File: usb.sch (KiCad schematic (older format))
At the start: 17 parts, among them J4 CONN_02X03, U1 LFE5U-85F-6BG381C, Y1 FNETHE025

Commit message: Adding default parts
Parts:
- D20, D21, D23, D24, D25, D26: footprint Diode_SMD:D_SOD-323_HandSoldering -> Diode_SMD:D_SOD-323
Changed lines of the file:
@@
 F 0 "D20" H 2800 2900 50  0000 C CNN
 F 1 "3.6V" H 2600 2910 50  0000 C CNN
-F 2 "Diode_SMD:D_SOD-323_HandSoldering" V 2600 3000 50  0001 C CNN
+F 2 "Diode_SMD:D_SOD-323" V 2600 3000 50  0001 C CNN
 F 3 "http://www.taiwansemi.com/products/datasheet/BZT52C2V4S%20SERIES_H1709.pdf" V 2600 3000 50  0001 C CNN
 F 4 "www.taiwansemi.com" H 2600 3000 60  0001 C CNN "MNF1_URL"
@@
 F 0 "D21" H 2900 3100 50  0000 C CNN
 F 1 "3.6V" H 2700 3100 50  0000 C CNN
-F 2 "Diode_SMD:D_SOD-323_HandSoldering" V 2700 3000 50  0001 C CNN
+F 2 "Diode_SMD:D_SOD-323" V 2700 3000 50  0001 C CNN
 F 3 "http://www.taiwansemi.com/products/datasheet/BZT52C2V4S%20SERIES_H1709.pdf" V 2700 3000 50  0001 C CNN
 F 4 "www.taiwansemi.com" H 2700 3000 60  0001 C CNN "MNF1_URL"
@@
 F 0 "D23" H 1650 4950 50  0000 C CNN
 F 1 "1N914" H 1900 4950 50  0000 C CNN
-F 2 "Diode_SMD:D_SOD-323_HandSoldering" V 1950 4850 50  0001 C CNN
+F 2 "Diode_SMD:D_SOD-323" V 1950 4850 50  0001 C CNN
 F 3 "https://www.diodes.com/assets/Datasheets/ds30065.pdf" V 1950 4850 50  0001 C CNN
 	1    1950 4850
@@
 F 0 "D25" H 1650 5550 50  0000 C CNN
 F 1 "1N914" H 1900 5550 50  0000 C CNN
-F 2 "Diode_SMD:D_SOD-323_HandSoldering" V 1950 5450 50  0001 C CNN
+F 2 "Diode_SMD:D_SOD-323" V 1950 5450 50  0001 C CNN
 F 3 "https://www.diodes.com/assets/Datasheets/ds30065.pdf" V 1950 5450 50  0001 C CNN
 	1    1950 5450
@@
 F 0 "D24" H 2250 4750 50  0000 C CNN
 F 1 "1N914" H 1900 4750 50  0000 C CNN
-F 2 "Diode_SMD:D_SOD-323_HandSoldering" V 1950 4650 50  0001 C CNN
+F 2 "Diode_SMD:D_SOD-323" V 1950 4650 50  0001 C CNN
 F 3 "https://www.diodes.com/assets/Datasheets/ds30065.pdf" V 1950 4650 50  0001 C CNN
 	1    1950 4650
@@
 F 0 "D26" H 2250 5350 50  0000 C CNN
 F 1 "1N914" H 1900 5350 50  0000 C CNN
-F 2 "Diode_SMD:D_SOD-323_HandSoldering" V 1950 5250 50  0001 C CNN
+F 2 "Diode_SMD:D_SOD-323" V 1950 5250 50  0001 C CNN
 F 3 "https://www.diodes.com/assets/Datasheets/ds30065.pdf" V 1950 5250 50  0001 C CNN
 F 4 "1N4148WS" H 1950 5250 50  0001 C CNN "MPN"

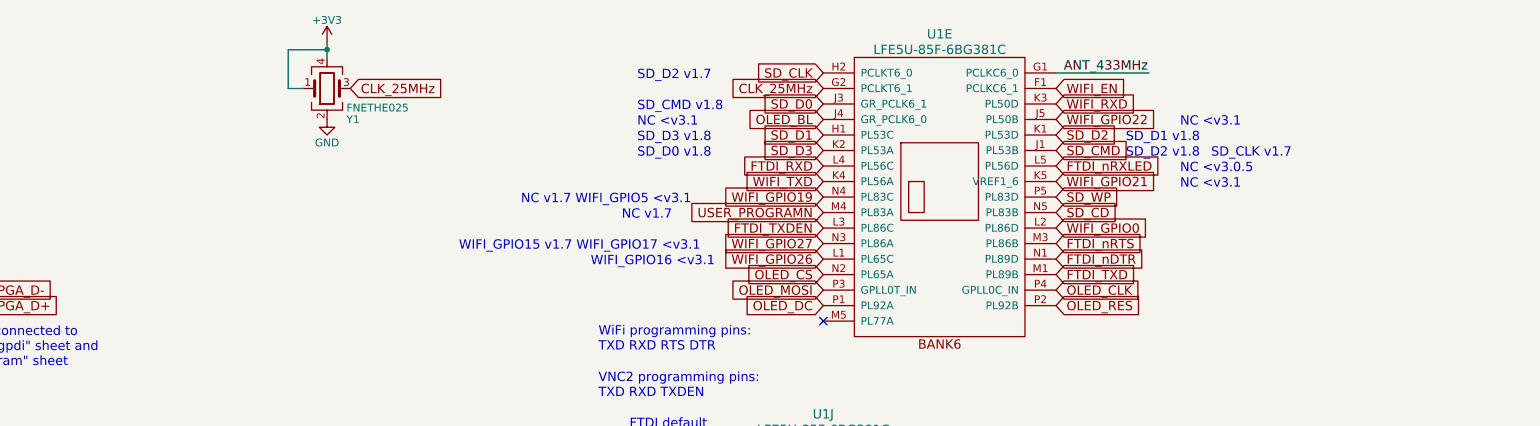
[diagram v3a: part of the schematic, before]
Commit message: Rewiering LCD OUT to bottom left
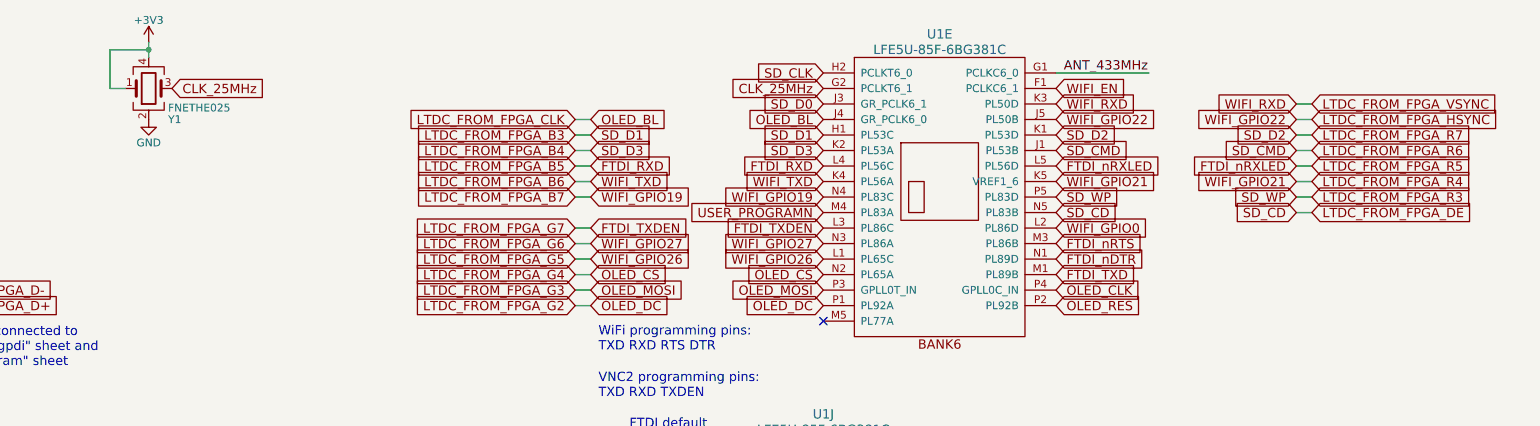
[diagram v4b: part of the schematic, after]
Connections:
- net OLED_BL renamed LTDC_FROM_FPGA_CLK
- net OLED_CS renamed LTDC_FROM_FPGA_G4
- net OLED_DC renamed LTDC_FROM_FPGA_G2
- net OLED_MOSI renamed LTDC_FROM_FPGA_G3
- net SD_CD renamed LTDC_FROM_FPGA_DE
- net SD_CMD renamed LTDC_FROM_FPGA_R6
- net SD_D1 renamed LTDC_FROM_FPGA_B3
- net SD_D2 renamed LTDC_FROM_FPGA_R7
- net SD_D3 renamed LTDC_FROM_FPGA_B4
- net SD_WP renamed LTDC_FROM_FPGA_R3
- net WIFI_GPIO19 renamed LTDC_FROM_FPGA_B7
- net WIFI_GPIO21 renamed LTDC_FROM_FPGA_R4
- net WIFI_GPIO22 renamed LTDC_FROM_FPGA_HSYNC
- net WIFI_GPIO26 renamed LTDC_FROM_FPGA_G5
- net WIFI_GPIO27 renamed LTDC_FROM_FPGA_G6
- net WIFI_RXD renamed LTDC_FROM_FPGA_VSYNC
- net WIFI_TXD renamed LTDC_FROM_FPGA_B6
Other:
- note removed: "NC <v3.0.5"
- note removed: "NC <v3.1"
- note removed: "NC v1.7"
- note removed: "NC v1.7 WIFI_GPIO5 <v3.1"
- note removed: "SD_CLK v1.7"
- note removed: "SD_CMD v1.8"
- note removed: "SD_D0 v1.8"
- note removed: "SD_D1 v1.8"
- note removed: "SD_D2 v1.7"
- note removed: "SD_D2 v1.8"
- note removed: "SD_D3 v1.8"
- note removed: "WIFI_GPIO15 v1.7 WIFI_GPIO17 <v3.1"
- note removed: "WIFI_GPIO16 <v3.1"
- moved on the sheet: Y1
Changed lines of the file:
@@
 L Device:Crystal_GND24 Y1
 U 1 1 5A079883
-P 5450 1450
-F 0 "Y1" H 5575 1650 50  0000 L CNN
-F 1 "FNETHE025" H 5575 1575 50  0000 L CNN
-F 2 "oscxo:Crystal_SMD_7050_4Pads" H 5450 1450 50  0001 C CNN
-F 3 "https://www.diodes.com/assets/Datasheets/FNETHE025.pdf" H 5450 1450 50  0001 C CNN
-F 4 "www.diodes.com" H 5450 1450 60  0001 C CNN "MNF1_URL"
-F 5 "FNETHE025" H 5450 1450 60  0001 C CNN "MPN"
-F 6 "SiT8008BC-81-33E-25.000000X" H 5450 1450 50  0001 C CNN "MPN2"
-F 7 "https://datasheet.lcsc.com/szlcsc/1912111437_Shenzhen-SCTF-Elec-S7D25-000000D20F30T_C387026.pdf" H 5450 1450 50  0001 C CNN "MNF3_URL"
-F 8 "S7D25.000000D20F30T" H 5450 1450 50  0001 C CNN "MPN3"
-F 9 "729-FNETHE025" H 5450 1450 60  0001 C CNN "Mouser"
-F 10 "788-8008BC8133E25X " H 5450 1450 50  0001 C CNN "Mouse_r2"
-F 11 "FNETHE025CT-ND" H 5450 1450 50  0001 C CNN "Digikey"
-F 12 "C390569" H 5450 1450 50  0001 C CNN "LCSC"
-F 13 "0.7942$" H 5450 1450 50  0001 C CNN "price100_Digikey"
-F 14 "FQ001" H 5450 1450 50  0001 C CNN "Koncar"
-F 15 "T" H 5450 1450 50  0001 C CNN "Side"
-	1    5450 1450
+P 4300 1450
+F 0 "Y1" H 4425 1650 50  0000 L CNN
+F 1 "FNETHE025" H 4425 1575 50  0000 L CNN
+F 2 "oscxo:Crystal_SMD_7050_4Pads" H 4300 1450 50  0001 C CNN
+F 3 "https://www.diodes.com/assets/Datasheets/FNETHE025.pdf" H 4300 1450 50  0001 C CNN
+F 4 "www.diodes.com" H 4300 1450 60  0001 C CNN "MNF1_URL"
+F 5 "FNETHE025" H 4300 1450 60  0001 C CNN "MPN"
+F 6 "SiT8008BC-81-33E-25.000000X" H 4300 1450 50  0001 C CNN "MPN2"
+F 7 "https://datasheet.lcsc.com/szlcsc/1912111437_Shenzhen-SCTF-Elec-S7D25-000000D20F30T_C387026.pdf" H 4300 1450 50  0001 C CNN "MNF3_URL"
+F 8 "S7D25.000000D20F30T" H 4300 1450 50  0001 C CNN "MPN3"
+F 9 "729-FNETHE025" H 4300 1450 60  0001 C CNN "Mouser"
+F 10 "788-8008BC8133E25X " H 4300 1450 50  0001 C CNN "Mouse_r2"
+F 11 "FNETHE025CT-ND" H 4300 1450 50  0001 C CNN "Digikey"
+F 12 "C390569" H 4300 1450 50  0001 C CNN "LCSC"
+F 13 "0.7942$" H 4300 1450 50  0001 C CNN "price100_Digikey"
+F 14 "FQ001" H 4300 1450 50  0001 C CNN "Koncar"
+F 15 "T" H 4300 1450 50  0001 C CNN "Side"
+	1    4300 1450
 	1    0    0    1
 $EndComp
 Wire Wire Line
-	5450 1150 5450 1200
-Wire Wire Line
-	5300 1450 5200 1450
-Wire Wire Line
-	5200 1450 5200 1200
-Wire Wire Line
-	5200 1200 5450 1200
-Connection ~ 5450 1200
+	4300 1150 4300 1200
+Wire Wire Line
+	4150 1450 4050 1450
+Wire Wire Line
+	4050 1450 4050 1200
+Wire Wire Line
+	4050 1200 4300 1200
+Connection ~ 4300 1200
 $Comp
 L power:GND #PWR0110
 U 1 1 5A07A1D3
-P 5450 1650
-F 0 "#PWR0110" H 5450 1400 50  0001 C CNN
-F 1 "GND" H 5450 1500 50  0000 C CNN
-F 2 "" H 5450 1650 50  0001 C CNN
-F 3 "" H 5450 1650 50  0001 C CNN
-	1    5450 1650
+P 4300 1650
+F 0 "#PWR0110" H 4300 1400 50  0001 C CNN
+F 1 "GND" H 4300 1500 50  0000 C CNN
+F 2 "" H 4300 1650 50  0001 C CNN
+F 3 "" H 4300 1650 50  0001 C CNN
+	1    4300 1650
 	1    0    0    -1
 $EndComp
-Text GLabel 5600 1450 2    60   Input ~ 0
+Text GLabel 4450 1450 2    60   Input ~ 0
 CLK_25MHz
 $Comp
 L power:+3V3 #PWR0109
 U 1 1 5A07A3D1
-P 5450 1150
-F 0 "#PWR0109" H 5450 1000 50  0001 C CNN
-F 1 "+3V3" H 5450 1290 50  0000 C CNN
-F 2 "" H 5450 1150 50  0001 C CNN
-F 3 "" H 5450 1150 50  0001 C CNN
-	1    5450 1150
+P 4300 1150
+F 0 "#PWR0109" H 4300 1000 50  0001 C CNN
+F 1 "+3V3" H 4300 1290 50  0000 C CNN
+F 2 "" H 4300 1150 50  0001 C CNN
+F 3 "" H 4300 1150 50  0001 C CNN
+	1    4300 1150
 	1    0    0    -1
 $EndComp
-Text Notes 6300 2500 0    60   ~ 0
-WIFI_GPIO15 v1.7 WIFI_GPIO17 <v3.1
 Text GLabel 8650 2150 0    60   Input ~ 0
 WIFI_GPIO19
 Text GLabel 8650 2450 0    60   Input ~ 0
 WIFI_GPIO27
-Text Notes 7450 1400 0    60   ~ 0
-SD_D2 v1.7
-Text Notes 11150 1900 0    60   ~ 0
-SD_CLK v1.7
 Text GLabel 1600 4850 0    60   Input ~ 0
 USB_FPGA_PULL_D+
@@
 	2700 2750 3000 2750
 Wire Wire Line
-	5450 1200 5450 1250
+	4300 1200 4300 1250
 Wire Wire Line
 	2550 4850 2750 4850
@@
 Text Label 1850 2650 0    60   ~ 0
 US2VBUS
-Text Notes 10600 1900 0    60   ~ 0
-SD_D2 v1.8
-Text Notes 10600 1800 0    60   ~ 0
-SD_D1 v1.8
-Text Notes 7450 1600 0    60   ~ 0
-SD_CMD v1.8
-Text Notes 7450 1800 0    60   ~ 0
-SD_D3 v1.8
-Text Notes 7450 1900 0    60   ~ 0
-SD_D0 v1.8
 Text GLabel 8650 1750 0    60   Input ~ 0
 SD_D1
@@
 Text GLabel 8650 2250 0    60   Input ~ 0
 USER_PROGRAMN
-Text Notes 7350 2300 0    60   ~ 0
-NC v1.7
 NoConn ~ 8650 2950
 Text GLabel 10150 1950 2    60   Input ~ 0
 FTDI_nRXLED
-Text Notes 10950 2000 0    60   ~ 0
-NC <v3.0.5
-Text Notes 6700 2200 0    60   ~ 0
-NC v1.7 WIFI_GPIO5 <v3.1
 Text GLabel 10150 2050 2    60   Input ~ 0
 WIFI_GPIO21
-Text Notes 10950 2100 0    60   ~ 0
-NC <v3.1
 Text GLabel 10150 1650 2    60   Input ~ 0
 WIFI_GPIO22
-Text Notes 10950 1700 0    60   ~ 0
-NC <v3.1
 Text GLabel 8650 1650 0    60   Input ~ 0
 OLED_BL
-Text Notes 7450 1700 0    60   ~ 0
-NC <v3.1
-Text Notes 7150 2600 0    60   ~ 0
-WIFI_GPIO16 <v3.1
+Text GLabel 7050 1750 0    60   Input ~ 0
+LTDC_FROM_FPGA_B3
+Text GLabel 7050 1850 0    60   Input ~ 0
+LTDC_FROM_FPGA_B4
+Text GLabel 7050 1950 0    60   Input ~ 0
+LTDC_FROM_FPGA_B5
+Text GLabel 7050 2050 0    60   Input ~ 0
+LTDC_FROM_FPGA_B6
+Text GLabel 7050 2150 0    60   Input ~ 0
+LTDC_FROM_FPGA_B7
+Text GLabel 11800 1750 2    60   Input ~ 0
+LTDC_FROM_FPGA_R7
+Text GLabel 11800 2150 2    60   Input ~ 0
+LTDC_FROM_FPGA_R3
+Text GLabel 11800 2050 2    60   Input ~ 0
+LTDC_FROM_FPGA_R4
+Text GLabel 11800 1950 2    60   Input ~ 0
+LTDC_FROM_FPGA_R5
+Text GLabel 11800 1850 2    60   Input ~ 0
+LTDC_FROM_FPGA_R6
+Text GLabel 7050 1650 0    60   Input ~ 0
+LTDC_FROM_FPGA_CLK
+Text GLabel 11800 1550 2    60   Input ~ 0
+LTDC_FROM_FPGA_VSYNC
+Text GLabel 11800 1650 2    60   Input ~ 0
+LTDC_FROM_FPGA_HSYNC
+Text GLabel 11800 2250 2    60   Input ~ 0
+LTDC_FROM_FPGA_DE
+Text GLabel 7050 2350 0    60   Input ~ 0
+LTDC_FROM_FPGA_G7
+Text GLabel 7050 2450 0    60   Input ~ 0
+LTDC_FROM_FPGA_G6
+Text GLabel 7050 2550 0    60   Input ~ 0
+LTDC_FROM_FPGA_G5
+Text GLabel 7050 2650 0    60   Input ~ 0
+LTDC_FROM_FPGA_G4
+Text GLabel 7050 2750 0    60   Input ~ 0
+LTDC_FROM_FPGA_G3
+Text GLabel 7050 2850 0    60   Input ~ 0
+LTDC_FROM_FPGA_G2
+Text GLabel 7150 1650 2    60   Input ~ 0
+OLED_BL
+Text GLabel 7150 1750 2    60   Input ~ 0
+SD_D1
+Text GLabel 7150 1850 2    60   Input ~ 0
+SD_D3
+Text GLabel 7150 1950 2    60   Input ~ 0
+FTDI_RXD
+Text GLabel 7150 2050 2    60   Input ~ 0
+WIFI_TXD
+Text GLabel 7150 2150 2    60   Input ~ 0
+WIFI_GPIO19
+Text GLabel 7150 2350 2    60   Input ~ 0
+FTDI_TXDEN
+Text GLabel 7150 2450 2    60   Input ~ 0
+WIFI_GPIO27
+Text GLabel 7150 2550 2    60   Input ~ 0
+WIFI_GPIO26
+Text GLabel 7150 2650 2    60   Input ~ 0
+OLED_CS
+Text GLabel 7150 2750 2    60   Input ~ 0
+OLED_MOSI
+Text GLabel 7150 2850 2    60   Input ~ 0
+OLED_DC
+Wire Wire Line
+	7050 1650 7150 1650
+Wire Wire Line
+	7050 1750 7150 1750
+Wire Wire Line
+	7050 1850 7150 1850
+Wire Wire Line
+	7050 1950 7150 1950
+Wire Wire Line
+	7050 2050 7150 2050
+Wire Wire Line
+	7050 2150 7150 2150
+Wire Wire Line
+	7050 2350 7150 2350
+Wire Wire Line
+	7050 2450 7150 2450
+Wire Wire Line
+	7150 2550 7050 2550
+Wire Wire Line
+	7050 2650 7150 2650
+Wire Wire Line
+	7050 2750 7150 2750
+Wire Wire Line
+	7150 2850 7050 2850
+Text GLabel 11700 1550 0    60   Input ~ 0
+WIFI_RXD
+Text GLabel 11700 1650 0    60   Input ~ 0
+WIFI_GPIO22
+Text GLabel 11700 1750 0    60   Input ~ 0
+SD_D2
+Text GLabel 11700 1850 0    60   Input ~ 0
+SD_CMD
+Text GLabel 11700 1950 0    60   Input ~ 0
+FTDI_nRXLED
+Text GLabel 11700 2050 0    60   Input ~ 0
+WIFI_GPIO21
+Text GLabel 11700 2150 0    60   Input ~ 0
+SD_WP
+Text GLabel 11700 2250 0    60   Input ~ 0
+SD_CD
+Wire Wire Line
+	11700 1550 11800 1550
+Wire Wire Line
+	11800 1650 11700 1650
+Wire Wire Line
+	11700 1750 11800 1750
+Wire Wire Line
+	11800 1850 11700 1850
+Wire Wire Line
+	11700 1950 11800 1950
+Wire Wire Line
+	11700 2050 11800 2050
+Wire Wire Line
+	11800 2150 11700 2150
+Wire Wire Line
+	11700 2250 11800 2250
 $EndSCHEMATC

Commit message: Update
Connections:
- net ANT_433MHz is gone; now on net LTDC_FROM_FPGA_R3: U1.G1 (PCLKC6_0)
- net LTDC_FROM_FPGA_G2 is gone; now on net LTDC_FROM_FPGA_B7: U1.P1 (PL92A)
- net LTDC_FROM_FPGA_G5 is gone; now on net LTDC_FROM_FPGA_B4: U1.L1 (PL65C)
- net LTDC_FROM_FPGA_HSYNC is gone; now on net LTDC_FROM_FPGA_R4: U1.J5 (PL50B)
- net LTDC_FROM_FPGA_B3: now also U1.N3 (PL86A); no longer U1.H1 (PL53C)
- net LTDC_FROM_FPGA_B4: no longer U1.K2 (PL53A)
- net LTDC_FROM_FPGA_B6: now also U1.N2 (PL65A); no longer U1.K4 (PL56A)
- net LTDC_FROM_FPGA_B7: no longer U1.N4 (PL83C)
- net LTDC_FROM_FPGA_G3: now also U1.H1 (PL53C); no longer U1.P3 (GPLL0T_IN)
- net LTDC_FROM_FPGA_G4: now also U1.K2 (PL53A); no longer U1.N2 (PL65A)
- net LTDC_FROM_FPGA_G6: now also U1.K4 (PL56A); no longer U1.N3 (PL86A)
- net LTDC_FROM_FPGA_R3: no longer U1.P5 (PL83D)
- net LTDC_FROM_FPGA_R4: no longer U1.K5 (VREF1_6)
- net LTDC_FROM_FPGA_VSYNC renamed WIFI_RXD
- new net LTDC_FROM_FPGA_B5: U1.P3 (GPLL0T_IN)
- new net LTDC_FROM_FPGA_G7: U1.N4 (PL83C)
- new net SD_WP: U1.P5 (PL83D)
- new net WIFI_GPIO21: U1.K5 (VREF1_6)
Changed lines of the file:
@@
 Text GLabel 8650 1650 0    60   Input ~ 0
 OLED_BL
-Text GLabel 7050 1750 0    60   Input ~ 0
+Text GLabel 7050 2450 0    60   Input ~ 0
 LTDC_FROM_FPGA_B3
-Text GLabel 7050 1850 0    60   Input ~ 0
+Text GLabel 7050 2550 0    60   Input ~ 0
 LTDC_FROM_FPGA_B4
-Text GLabel 7050 1950 0    60   Input ~ 0
-LTDC_FROM_FPGA_B5
-Text GLabel 7050 2050 0    60   Input ~ 0
+Text GLabel 7050 2650 0    60   Input ~ 0
 LTDC_FROM_FPGA_B6
-Text GLabel 7050 2150 0    60   Input ~ 0
-LTDC_FROM_FPGA_B7
 Text GLabel 11800 1750 2    60   Input ~ 0
 LTDC_FROM_FPGA_R7
-Text GLabel 11800 2150 2    60   Input ~ 0
-LTDC_FROM_FPGA_R3
-Text GLabel 11800 2050 2    60   Input ~ 0
+Text GLabel 11800 1650 2    60   Input ~ 0
 LTDC_FROM_FPGA_R4
 Text GLabel 11800 1950 2    60   Input ~ 0
@@
 Text GLabel 7050 1650 0    60   Input ~ 0
 LTDC_FROM_FPGA_CLK
-Text GLabel 11800 1550 2    60   Input ~ 0
-LTDC_FROM_FPGA_VSYNC
-Text GLabel 11800 1650 2    60   Input ~ 0
-LTDC_FROM_FPGA_HSYNC
 Text GLabel 11800 2250 2    60   Input ~ 0
 LTDC_FROM_FPGA_DE
+Text GLabel 7050 2150 0    60   Input ~ 0
+LTDC_FROM_FPGA_G7
+Text GLabel 7050 2050 0    60   Input ~ 0
+LTDC_FROM_FPGA_G6
+Text GLabel 7050 1950 0    60   Input ~ 0
+LTDC_FROM_FPGA_G5
+Text GLabel 7050 1850 0    60   Input ~ 0
+LTDC_FROM_FPGA_G4
+Text GLabel 7050 1750 0    60   Input ~ 0
+LTDC_FROM_FPGA_G3
 Text GLabel 7050 2350 0    60   Input ~ 0
-LTDC_FROM_FPGA_G7
-Text GLabel 7050 2450 0    60   Input ~ 0
-LTDC_FROM_FPGA_G6
-Text GLabel 7050 2550 0    60   Input ~ 0
-LTDC_FROM_FPGA_G5
-Text GLabel 7050 2650 0    60   Input ~ 0
-LTDC_FROM_FPGA_G4
-Text GLabel 7050 2750 0    60   Input ~ 0
-LTDC_FROM_FPGA_G3
-Text GLabel 7050 2850 0    60   Input ~ 0
 LTDC_FROM_FPGA_G2
 Text GLabel 7150 1650 2    60   Input ~ 0
@@
 Wire Wire Line
 	7150 2850 7050 2850
-Text GLabel 11700 1550 0    60   Input ~ 0
-WIFI_RXD
 Text GLabel 11700 1650 0    60   Input ~ 0
 WIFI_GPIO22
@@
 Text GLabel 11700 1950 0    60   Input ~ 0
 FTDI_nRXLED
-Text GLabel 11700 2050 0    60   Input ~ 0
-WIFI_GPIO21
-Text GLabel 11700 2150 0    60   Input ~ 0
-SD_WP
 Text GLabel 11700 2250 0    60   Input ~ 0
 SD_CD
-Wire Wire Line
-	11700 1550 11800 1550
 Wire Wire Line
 	11800 1650 11700 1650
@@
 	11700 1950 11800 1950
 Wire Wire Line
-	11700 2050 11800 2050
-Wire Wire Line
-	11800 2150 11700 2150
-Wire Wire Line
 	11700 2250 11800 2250
+Text GLabel 10750 1350 2    60   Input ~ 0
+LTDC_FROM_FPGA_R3
+Text GLabel 7050 2750 0    60   Input ~ 0
+LTDC_FROM_FPGA_B5
+Text GLabel 7050 2850 0    60   Input ~ 0
+LTDC_FROM_FPGA_B7
 $EndSCHEMATC
